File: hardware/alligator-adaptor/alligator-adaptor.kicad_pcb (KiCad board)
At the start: 2 copper layers, 21 parts, among them P1 CONN_01X04, P10 CONN_01X01, P11 CONN_02X10, P12 CONN_01X01, P13 CONN_01X01, P14 CONN_01X04, P15 CONN_01X04, P16 CONN_01X04, P17 CONN_01X04, P18 CONN_01X04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

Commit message: First cut.  Routed, zone filled.  Plots generated.
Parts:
- added P22: CONN_01X01, Mounting_Holes:MountingHole_3mm_Pad, F.Cu at (92.2, 51.0)
- added P23: CONN_01X01, Mounting_Holes:MountingHole_3mm_Pad, F.Cu at (77.2, 81.0)
- P11, P5: moved to B.Cu
- P3, P4, P6, P7: footprint Mounting_Holes:MountingHole_3.2mm_M3_Pad_Via -> Mounting_Holes:MountingHole_3.2mm_M3_Pad
- moved P2 69.2 mm to (69.6, 105.5), turned to 90 degrees
- moved P5 67.4 mm to (72.9, 100.5)
- moved P8 65.3 mm to (77.2, 94.7), turned to 270 degrees
- moved P13 59.4 mm to (76.0, 86.0)
- moved P12 53.3 mm to (93.5, 86.0)
- moved P10 27.3 mm to (76.0, 46.0)
- moved P11 22.4 mm to (84.8, 36.1), turned to 90 degrees
- moved P9 9.14 mm to (93.5, 46.0)
- moved P1 6.73 mm to (110.4, 40.9)
- moved P14 6.73 mm to (110.4, 62.5)
- moved P15 6.73 mm to (110.4, 84.1)
- moved P16 6.73 mm to (110.4, 105.7)
- moved P17 6.73 mm to (110.4, 127.5)
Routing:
- net GND: track 0.00 -> 249.7 mm
- net +24V: track 0.00 -> 222.8 mm
- net Net-(P11-Pad9): track 0.00 -> 105.1 mm
- net Net-(P11-Pad10): track 0.00 -> 102.0 mm
- net Net-(P11-Pad7): track 0.00 -> 101.3 mm, vias 0 -> 1
- net Net-(P11-Pad8): track 0.00 -> 94.3 mm
- net Net-(P11-Pad12): track 0.00 -> 84.9 mm
- net Net-(P11-Pad4): track 0.00 -> 72.9 mm
- net Net-(P11-Pad11): track 0.00 -> 72.0 mm
- net Net-(P11-Pad1): track 0.00 -> 69.1 mm, vias 0 -> 1
- net +12V: track 0.00 -> 62.1 mm
- net Net-(P11-Pad6): track 0.00 -> 54.6 mm, vias 0 -> 1
- net Net-(P11-Pad17): track 0.00 -> 53.0 mm
- net Net-(P11-Pad15): track 0.00 -> 48.9 mm, vias 0 -> 1
- net Net-(P11-Pad2): track 0.00 -> 44.5 mm
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- added copper zone on B.Cu, net +24V
- added copper zone on F.Cu, net GND
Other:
- board outline added: 64.5 x 107.2 mm
- net class Default: clearance 0.2 -> 0.3; trace_width 0.25 -> 0.45
- net class power added: clearance 0.3, trace_width 2.5, via_dia 0.6, via_drill 0.4
- rule trace_clearance: 0.2 -> 0.3

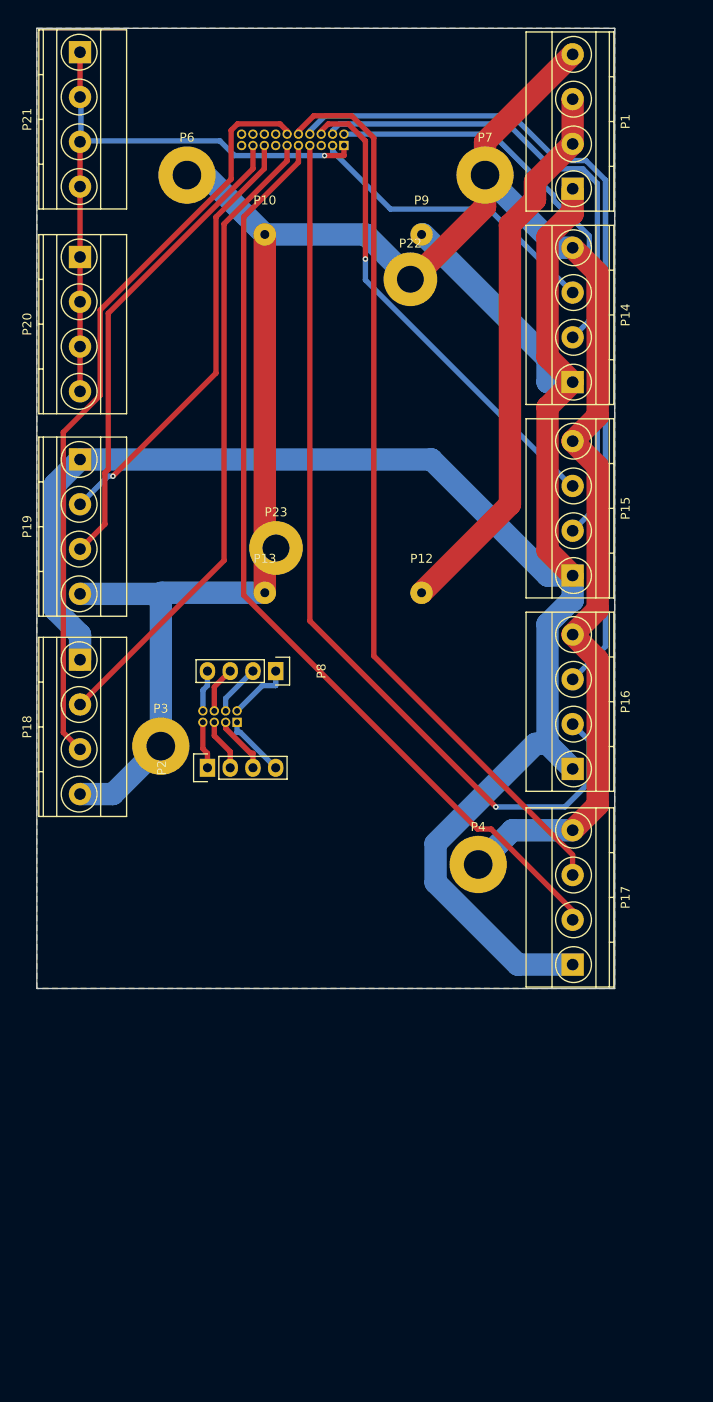
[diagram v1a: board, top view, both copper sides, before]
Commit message: Relocate pin headers for Alligator Board.  Relocate stepper enable connectors to be furthest from the connector and reduce overall size of board.
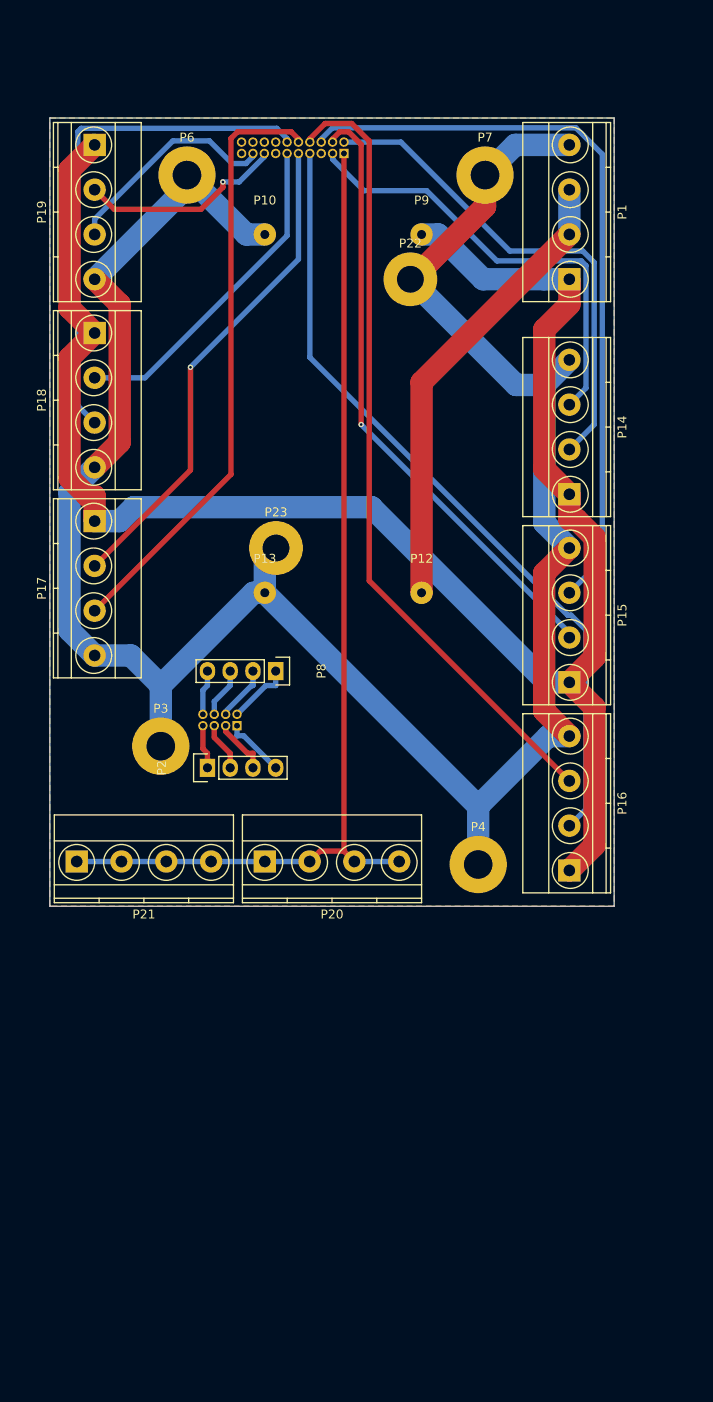
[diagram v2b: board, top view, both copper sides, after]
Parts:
- moved P21 90.3 mm to (55.0, 116.0), turned to 0 degrees
- moved P17 72.8 mm to (57.0, 78.0), turned to 270 degrees
- moved P20 70.6 mm to (76.0, 116.0), turned to 0 degrees
- moved P18 36.5 mm to (57.0, 57.0)
- moved P19 35.2 mm to (57.0, 36.0)
- moved P14 12.5 mm to (110.0, 75.0)
- moved P15 11.9 mm to (110.0, 96.0)
- moved P16 11.3 mm to (110.0, 117.0)
- moved P1 10.1 mm to (110.0, 51.0)
- moved P11 0.89 mm to (84.8, 37.0)
- moved P5 0.38 mm to (72.9, 100.8)
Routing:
- net Net-(P11-Pad9): track 105.1 -> 55.5 mm, vias 0 -> 1
- net Net-(P11-Pad1): track 69.1 -> 114.8 mm, vias 1 -> 0
- net Net-(P11-Pad11): track 72.0 -> 37.2 mm
- net Net-(P11-Pad10): track 102.0 -> 67.5 mm
- net Net-(P11-Pad6): track 54.6 -> 83.9 mm, vias 1 -> 0
- net Net-(P11-Pad17): track 53.0 -> 24.7 mm
- net Net-(P11-Pad12): track 84.9 -> 57.6 mm
- net Net-(P11-Pad15): track 48.9 -> 23.0 mm
- net +24V: track 222.8 -> 201.0 mm
- net Net-(P11-Pad3): track 34.0 -> 50.1 mm
- net Net-(P11-Pad7): track 101.3 -> 88.8 mm, vias 1 -> 0
- net Net-(P11-Pad2): track 44.5 -> 55.5 mm
- net +12V: track 62.1 -> 51.8 mm
- net GND: track 249.7 -> 256.7 mm
- net Net-(P11-Pad8): track 94.3 -> 89.2 mm
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- added copper zone on F.Cu, net +24V
- added copper zone on B.Cu, net GND
- removed copper zone on B.Cu, net +24V
- removed copper zone on F.Cu, net GND
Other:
- board size 64.5 x 107.2 mm -> 63 x 88 mm
